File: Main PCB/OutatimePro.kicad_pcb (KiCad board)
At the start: 2 copper layers, 25.7 x 27.7 mm, 48 parts, among them IC1 PAM8904JPR, J1 USB_B_Micro_PCB_Edge_receptac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, J2 FH35C-9S-0.3SHW, J3 OSO_SWD, Q1 ALS-PT19-315C/L177/TR8, SW1 EVPAWED40, U1 ATSAML22N18A-CFUT, U2 MIC5365-3.3YMT, U3 USBLC6-2P6, U4 MAX40200ANS, Y1 32.768kHz

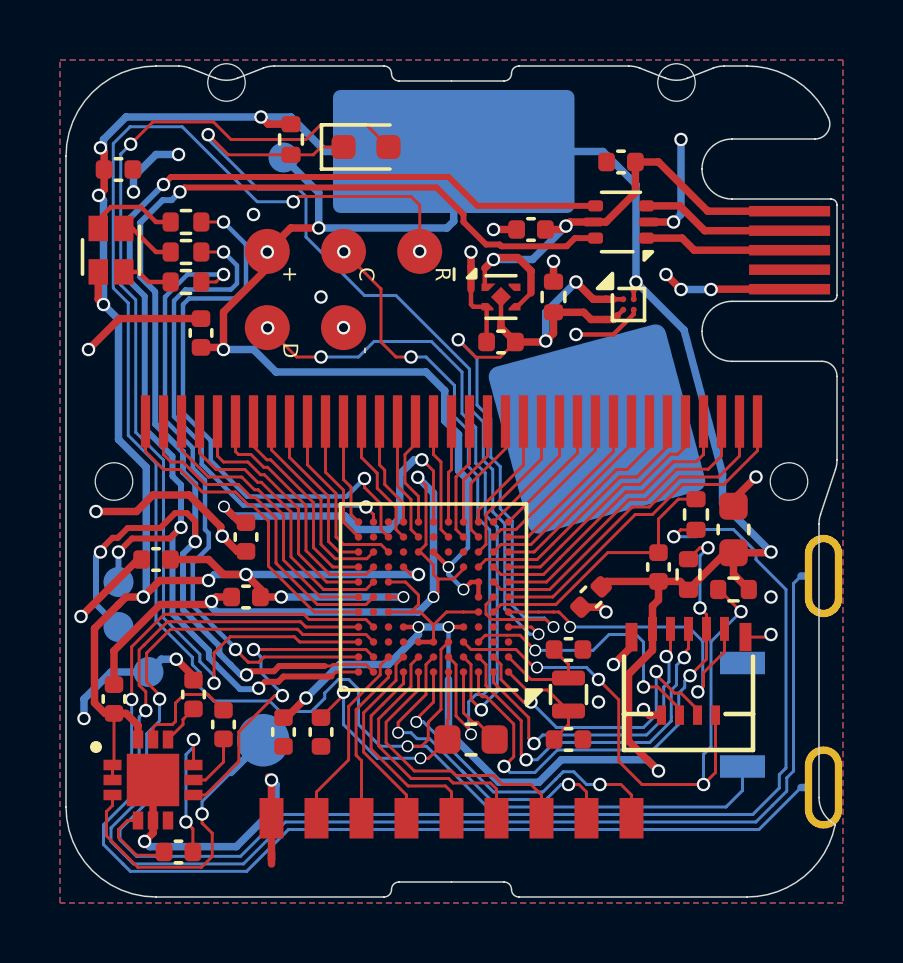
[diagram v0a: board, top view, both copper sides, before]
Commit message: Change keypad/button pins for available interrupts
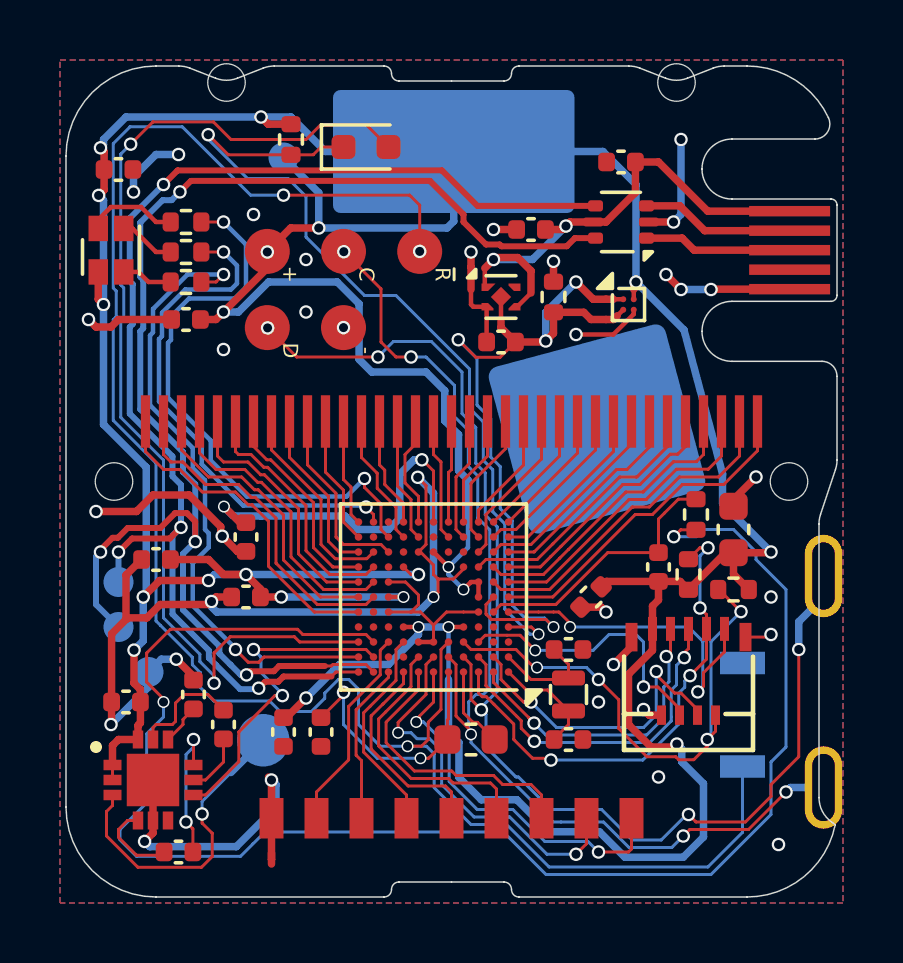
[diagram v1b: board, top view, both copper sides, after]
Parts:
- moved C10 0.67 mm to (17.0, 21.8), turned to 180 degrees
- moved C17 0.41 mm to (15.0, 34.5), turned to 0 degrees
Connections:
- J3 pad 1: /SWDIO -> /BTN_MODE
- J3 pad 4: /SWCLK -> /BTN_ADJUST
- U1 pad B4: /SWDIO -> /BTN_MODE
- U1 pad B5: /SWCLK -> /BTN_ADJUST
- U1 pad B8: /KPD_R2 -> unconnected-(U1-PC25/INT1/COM0.3+4.3-PadB8)
- U1 pad B9: /KPD_R4 -> unconnected-(U1-PC24/INT0/COM0.2+4.2-PadB9)
- U1 pad C8: unconnected-(U1-PB25/INT9/COM0.1+4.1-PadC8) -> /KPD_R2
- U1 pad C9: unconnected-(U1-PB24/INT8/COM0.0+4.0-PadC9) -> /KPD_R4
- U1 pad D10: /BTN_ADJUST -> unconnected-(U1-PB19/INT3/COM5.3+3.3/SLCD45-PadD10)
- U1 pad D11: /BTN_MODE -> unconnected-(U1-PB20/INT4/COM3.0+5.0/SLCD46-PadD11)
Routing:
- net /SWCLK: track 22.1 -> 0.00 mm, vias 3 -> 0
- net /SWDIO: track 21.5 -> 0.00 mm, vias 3 -> 0
- net VCC: track 150.0 -> 155.7 mm, vias 21 -> 22
- net /BTN_ADJUST: track 41.2 -> 36.4 mm, vias 1 -> 5
- net /BTN_MODE: track 46.7 -> 42.5 mm, vias 1 -> 5
- net /SCL: track 21.0 -> 17.4 mm
- net /~{RESET}: track 59.3 -> 62.4 mm
- net /~{TS_ENABLE}: track 50.5 -> 52.2 mm
- net /SDA: track 17.8 -> 16.5 mm
- net /KPD_C4: track 11.4 -> 12.6 mm
- net /KPD_C3: track 11.7 -> 12.6 mm
- net GND: track 82.1 -> 81.2 mm, vias 32 -> 35
- net /A4/D1/MISO: track 10.8 -> 10.1 mm
- net /A2_MOSI: track 12.8 -> 12.3 mm
- net /KPD_R4: track 6.37 -> 6.87 mm
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
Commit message: rename seg/com numbers to reflect firmware, fix up batt/vcc change circuitry
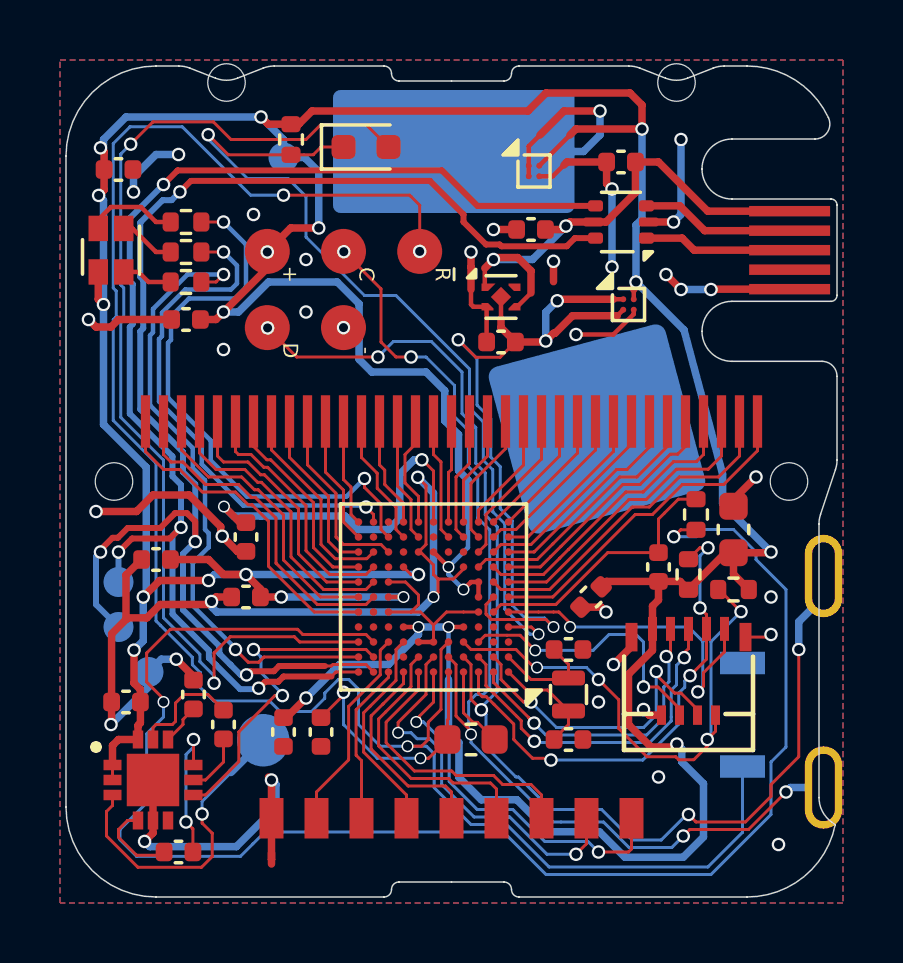
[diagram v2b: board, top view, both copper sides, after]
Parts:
- removed R8: 10k, Resistor_SMD:R_0402_1005Metric
- added U5: MAX40200ANS, Package_BGA:WLP-4_0.728x0.728mm_Layout2x2_P0.35mm, F.Cu at (28.6, 16.8)
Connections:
- BRD1 pad 1: VCC -> +BATT
- KPD1 pad 2: /KPD_R4 -> /KPD_R3
- KPD1 pad 3: /KPD_R3 -> /KPD_R2
- KPD1 pad 4: /KPD_R2 -> /KPD_R1
- KPD1 pad 5: /KPD_R1 -> /KPD_R0
- KPD1 pad 6: /KPD_C1 -> /KPD_C0
- KPD1 pad 7: /KPD_C2 -> /KPD_C1
- KPD1 pad 8: /KPD_C3 -> /KPD_C2
- KPD1 pad 9: /KPD_C4 -> /KPD_C3
- LCD1 pad 1: /COM0 -> /LCD_NC
- LCD1 pad 10: /SEG06 -> /SEG05
- LCD1 pad 11: /SEG07 -> /SEG06
- LCD1 pad 12: /SEG08 -> /SEG07
- LCD1 pad 13: /SEG09 -> /SEG08
- LCD1 pad 14: /SEG10 -> /SEG09
- LCD1 pad 15: /SEG11 -> /SEG10
- LCD1 pad 16: /SEG12 -> /SEG11
- LCD1 pad 17: /SEG13 -> /SEG12
- LCD1 pad 18: /SEG14 -> /SEG13
- LCD1 pad 19: /SEG15 -> /SEG14
- LCD1 pad 2: /COM1 -> /COM0
- LCD1 pad 20: /SEG16 -> /SEG15
- LCD1 pad 21: /SEG17 -> /SEG16
- LCD1 pad 22: /SEG18 -> /SEG17
- LCD1 pad 23: /SEG19 -> /SEG18
- LCD1 pad 24: /SEG20 -> /SEG19
- LCD1 pad 25: /SEG21 -> /SEG20
- LCD1 pad 26: /SEG22 -> /SEG21
- LCD1 pad 27: /SEG23 -> /SEG22
- LCD1 pad 28: /SEG24 -> /SEG23
- LCD1 pad 29: /SEG25 -> /SEG24
- LCD1 pad 3: /COM2 -> /COM1
- LCD1 pad 30: /SEG26 -> /SEG25
- LCD1 pad 31: /SEG27 -> /SEG26
- LCD1 pad 32: /SEG28 -> /SEG27
- LCD1 pad 33: /SEG29 -> /SEG28
- LCD1 pad 34: /SEG30 -> /SEG39
- LCD1 pad 35: /SEG31 -> /SEG30
- LCD1 pad 4: /COM3 -> /COM2
- LCD1 pad 5: /SEG01 -> /SEG00
- LCD1 pad 6: /SEG02 -> /SEG01
- LCD1 pad 7: /SEG03 -> /SEG02
- LCD1 pad 8: /SEG04 -> /SEG03
- LCD1 pad 9: /SEG05 -> /SEG04
- U1 pad A6: /KPD_C4 -> /KPD_C3
- U1 pad A7: /KPD_C2 -> /KPD_C1
- U1 pad A8: /KPD_R1 -> /KPD_R0
- U1 pad A9: /KPD_R3 -> /KPD_R2
- U1 pad B6: /KPD_C3 -> /KPD_C2
- U1 pad B7: /KPD_C1 -> /KPD_C0
- U1 pad C8: /KPD_R2 -> /KPD_R1
- U1 pad C9: /KPD_R4 -> /KPD_R3
- U1 pad E11: /COM0 -> /LCD_NC
- U1 pad F1: /SEG31 -> /SEG30
- U1 pad F10: /COM1 -> /COM0
- U1 pad F11: /COM2 -> /COM1
- U1 pad G1: /SEG29 -> /SEG28
- U1 pad G10: /COM3 -> /COM2
- U1 pad G11: /SEG01 -> /SEG00
- U1 pad G2: /SEG30 -> /SEG29
- U1 pad H1: /SEG27 -> /SEG26
- U1 pad H10: /SEG02 -> /SEG01
- U1 pad H11: /SEG03 -> /SEG02
- U1 pad H2: /SEG28 -> /SEG27
- U1 pad H3: /SEG26 -> /SEG25
- U1 pad J1: /SEG25 -> /SEG24
- U1 pad J10: /SEG04 -> /SEG03
- U1 pad J11: /SEG05 -> /SEG04
- U1 pad J2: /SEG24 -> /SEG23
- U1 pad J3: /SEG19 -> /SEG18
- U1 pad J9: /SEG06 -> /SEG05
- U1 pad K1: /SEG23 -> /SEG22
- U1 pad K11: /SEG07 -> /SEG06
- U1 pad K2: /SEG22 -> /SEG21
- U1 pad K3: /SEG17 -> /SEG16
- U1 pad K4: /SEG15 -> /SEG14
- U1 pad K5: /SEG13 -> /SEG12
- U1 pad K7: /SEG11 -> /SEG10
- U1 pad K8: /SEG09 -> /SEG08
- U1 pad L1: /SEG21 -> /SEG20
- U1 pad L11: /SEG08 -> /SEG07
- U1 pad L2: /SEG20 -> /SEG19
- U1 pad L3: /SEG18 -> /SEG17
- U1 pad L4: /SEG16 -> /SEG15
- U1 pad L5: /SEG14 -> /SEG13
- U1 pad L7: /SEG12 -> /SEG11
- U1 pad L8: /SEG10 -> /SEG09
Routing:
- net /KPD_C4: track 12.6 -> 0.00 mm, vias 2 -> 0
- net /SEG31: track 11.3 -> 0.00 mm
- net /LCD_NC: track 0.00 -> 11.2 mm
- net +BATT: track 0.00 -> 9.76 mm, vias 0 -> 1
- net /COM3: track 9.72 -> 0.00 mm
- net /KPD_C0: track 0.00 -> 9.01 mm
- net /SEG00: track 0.00 -> 8.47 mm
- net /KPD_R0: track 0.00 -> 7.16 mm
- net /KPD_R4: track 6.87 -> 0.00 mm
- net GND: track 81.2 -> 87.2 mm, vias 35 -> 37
- net /KPD_C2: track 9.48 -> 12.6 mm, vias 0 -> 2
- net /SEG06: track 6.20 -> 4.31 mm
- net /SEG25: track 7.00 -> 8.80 mm
- net /KPD_R2: track 7.02 -> 5.40 mm
- net /KPD_R3: track 5.40 -> 6.87 mm
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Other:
- board text added: "v260902"
- board text removed: "no usb with batt!!"
- board text removed: "v260827"

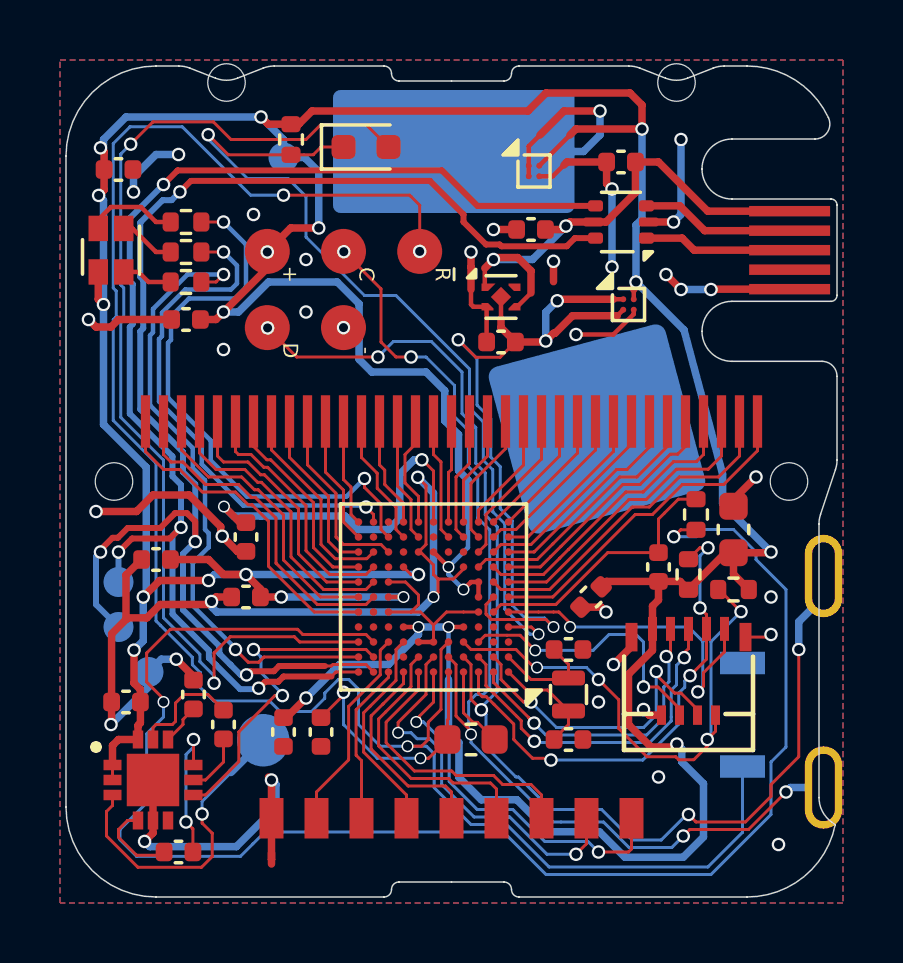
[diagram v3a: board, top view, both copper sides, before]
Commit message: Remove FPC connector, put IMU on main pcb
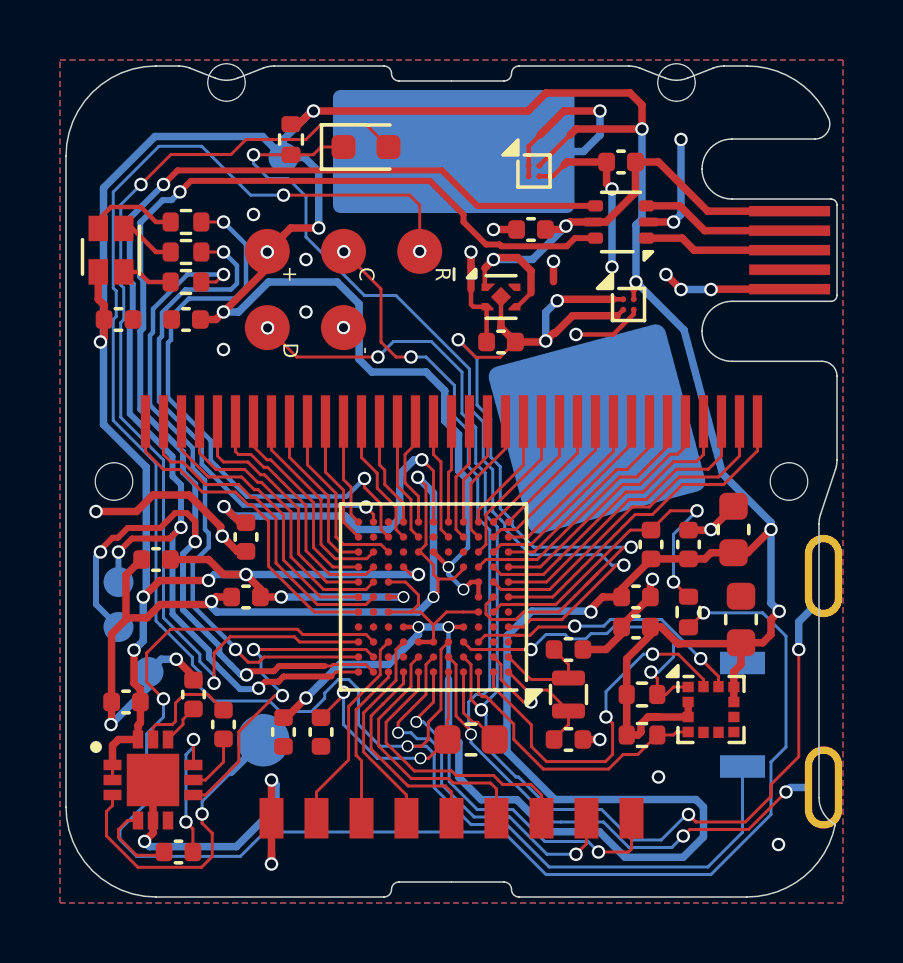
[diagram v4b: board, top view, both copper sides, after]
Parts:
- removed J2: FH35C-9S-0.3SHW, OutatimePro:FH35-9S-0.3SHW
- added C19: 0.1uF, Capacitor_SMD:C_0402_1005Metric, F.Cu at (32.0, 32.0)
- added C20: 10uF, Capacitor_SMD:C_0603_1608Metric, F.Cu at (35.5, 31.8)
- added C21: 0.1uF, Capacitor_SMD:C_0402_1005Metric, F.Cu at (33.8, 29.2)
- added U6: LIS2DW12TR, OutatimePro:LGA-12_2x2mm_P0.5mm, F.Cu at (34.5, 34.8)
- moved R6 5.57 mm to (32.2, 35.6), turned to 0 degrees
- moved C18 5.00 mm to (14.8, 21.8)
- moved R7 4.64 mm to (32.2, 34.2), turned to 0 degrees
- moved R5 3.26 mm to (33.8, 31.5)
- moved C9 1.50 mm to (32.0, 31.0), turned to 0 degrees
- moved TH1 0.79 mm to (32.5, 29.2)
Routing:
- net VCC: track 156.4 -> 177.6 mm, vias 23 -> 22
- net /A2_MOSI: track 12.3 -> 0.00 mm, vias 2 -> 0
- net /A0: track 11.2 -> 0.00 mm, vias 2 -> 0
- net /A1_SCK: track 10.6 -> 2.16 mm, vias 2 -> 1
- net /SDA: track 16.5 -> 9.55 mm, vias 4 -> 0
- net /SCL: track 17.4 -> 11.2 mm, vias 4 -> 2
- net +3.3V: track 26.2 -> 30.2 mm
- net GND: track 87.2 -> 83.3 mm, vias 37 -> 31
- net /~{TS_ENABLE}: track 52.2 -> 48.7 mm
- net /TEMPSENSE: track 8.96 -> 11.6 mm, vias 0 -> 2
- net /A4/D1/MISO: track 10.1 -> 12.6 mm
- net /~{RESET}: track 62.4 -> 60.9 mm
- net /~{LS_ENABLE}: track 35.3 -> 33.8 mm

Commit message: Add test points to break out A1/A2
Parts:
- added TP5: PB01, OutatimePro:TestPoint_Pad_D1.0mm, B.Cu at (34.8, 38.5)
- added TP6: PB02, OutatimePro:TestPoint_Pad_D1.0mm, B.Cu at (32.2, 38.5)
- moved C2 0.25 mm to (30.0, 35.8)
- moved C3 0.25 mm to (30.0, 32.8)
- moved Y1 0.25 mm to (30.0, 34.2)
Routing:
- net VCC: track 177.6 -> 164.8 mm, vias 22 -> 24
- net /A2_MOSI: track 0.00 -> 8.52 mm, vias 0 -> 1
- net /A1_SCK: track 2.16 -> 10.6 mm
- net GND: track 83.3 -> 86.5 mm, vias 31 -> 34
- net /A4/D1/MISO: track 12.6 -> 13.4 mm
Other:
- board text added: "A1"
- board text added: "A2"
- board text added: "v260907"
- board text removed: "OUTATIME"
- board text removed: "v260902"
